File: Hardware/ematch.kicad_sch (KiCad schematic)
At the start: 33 parts, among them J3 Conn_01x02_Male, J4 Conn_01x02_Male, J5 Conn_01x02_Male, J6 Conn_01x02_Male, Q1 NCV8403, Q2 NCV8403, Q3 NCV8403, Q4 NCV8403, U6 LTV-247

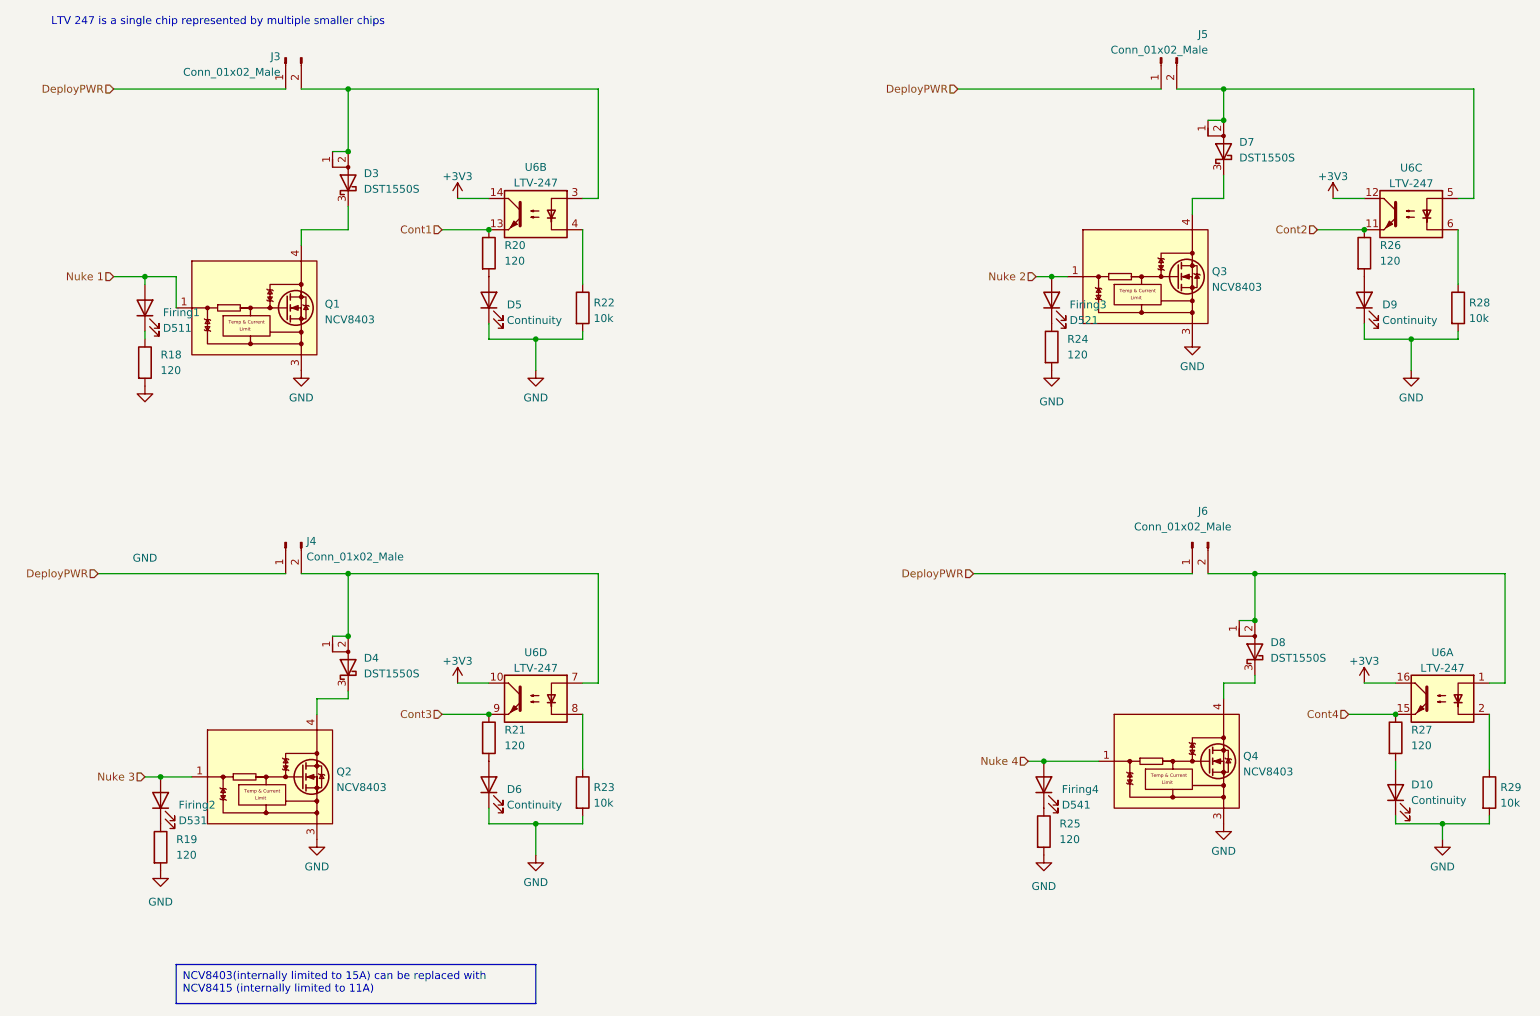
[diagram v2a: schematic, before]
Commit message: high V side finished, CAN circuit and ESP left to place
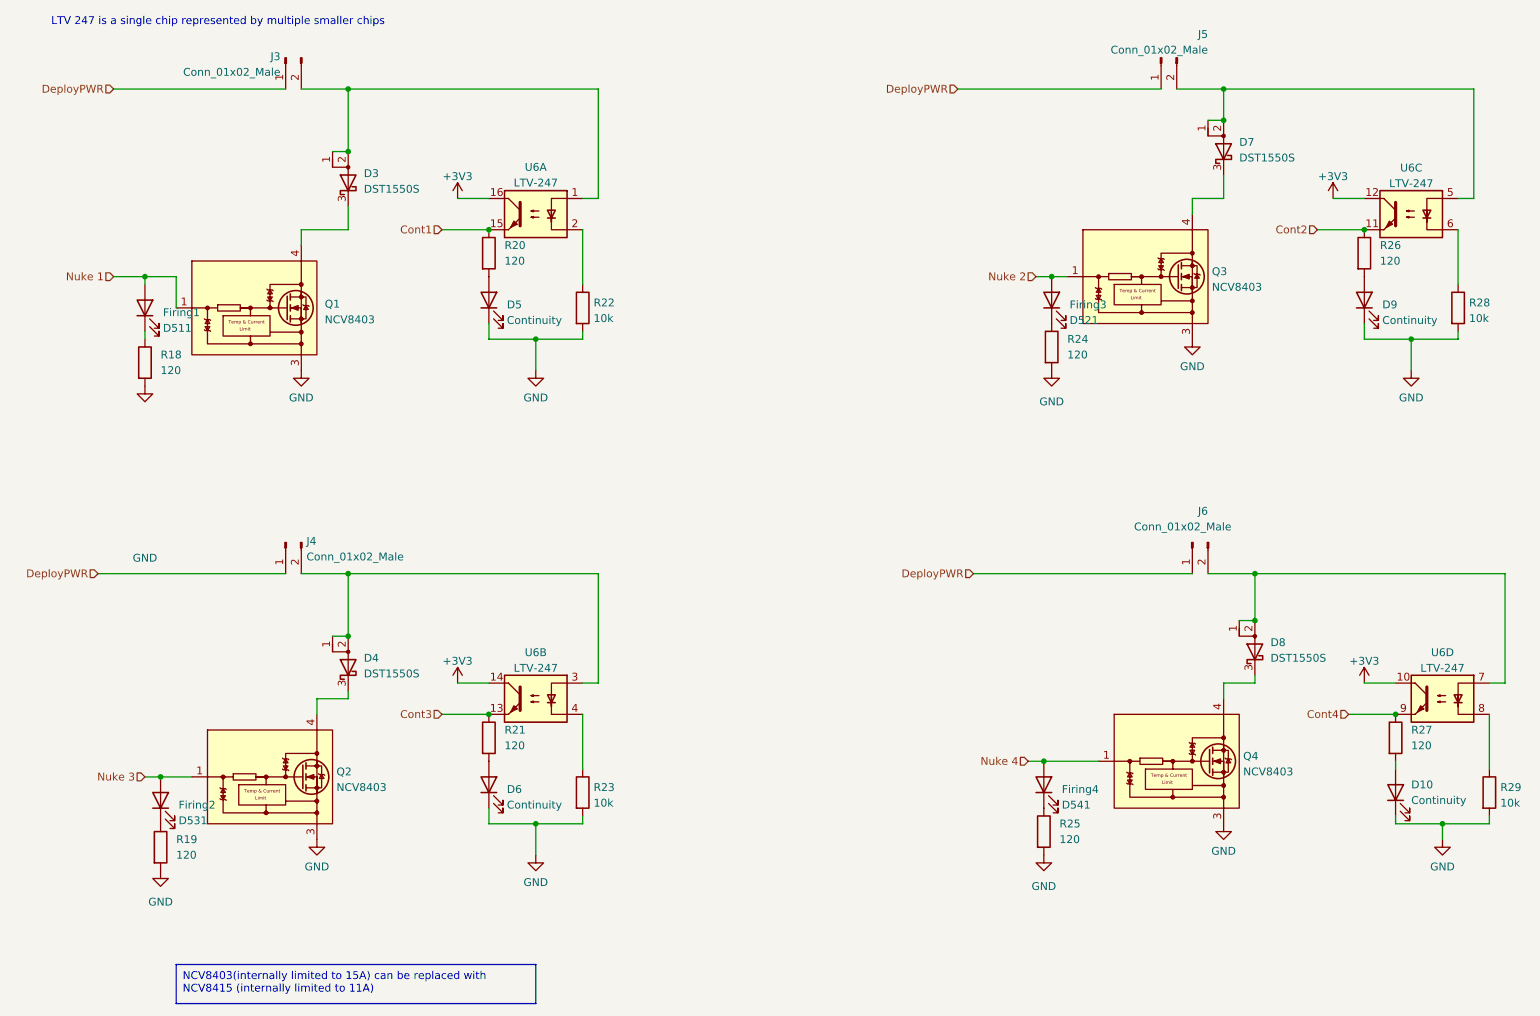
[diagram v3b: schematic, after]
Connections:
- net +3V3: now also U6.10, U6.14, U6.16; no longer U6.10, U6.14, U6.16
- net Cont1: now also U6.15; no longer U6.13
- net Cont3: now also U6.13; no longer U6.9
- net Cont4: now also U6.9; no longer U6.15
- net at D3.1 (A), D3.2 (A), J3.2 (Pin_2): now also U6.1; no longer U6.3
- net at D4.1 (A), D4.2 (A), J4.2 (Pin_2): now also U6.3; no longer U6.7
- net at D8.1 (A), D8.2 (A), J6.2 (Pin_2): now also U6.7; no longer U6.1
- net at R29.1: now also U6.8; no longer U6.2
- net at R23.1: now also U6.4; no longer U6.8
- net at R22.1: now also U6.2; no longer U6.4
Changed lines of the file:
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@@
     )
   )
-  (symbol (lib_id "Isolator:LTV-247") (at 243.84 129.54 0) (mirror y) (unit 1)
+  (symbol (lib_id "Isolator:LTV-247") (at 243.84 129.54 0) (mirror y) (unit 4)
     (in_bom yes) (on_board yes) (dnp no) (fields_autoplaced)
     (property "Reference" "U6" (at 243.84 122.0302 0)
@@
       (project "flintandsteel"
         (path "/7db990e4-92e1-4f99-b4d2-435bbec1ba83/b9a85f03-bf97-4e73-b79c-bd8547648cfe"
-          (reference "U6") (unit 1)
+          (reference "U6") (unit 4)
         )
       )
@@
     )
   )
-  (symbol (lib_id "Isolator:LTV-247") (at 96.52 50.8 0) (mirror y) (unit 2)
+  (symbol (lib_id "Isolator:LTV-247") (at 96.52 50.8 0) (mirror y) (unit 1)
     (in_bom yes) (on_board yes) (dnp no) (fields_autoplaced)
     (property "Reference" "U6" (at 96.52 43.18 0)
@@
       (project "flintandsteel"
         (path "/7db990e4-92e1-4f99-b4d2-435bbec1ba83/b9a85f03-bf97-4e73-b79c-bd8547648cfe"
-          (reference "U6") (unit 2)
+          (reference "U6") (unit 1)
         )
       )
@@
     )
   )
-  (symbol (lib_id "Isolator:LTV-247") (at 96.52 129.54 0) (mirror y) (unit 4)
+  (symbol (lib_id "Isolator:LTV-247") (at 96.52 129.54 0) (mirror y) (unit 2)
     (in_bom yes) (on_board yes) (dnp no) (fields_autoplaced)
     (property "Reference" "U6" (at 96.52 122.0302 0)
@@
       (project "flintandsteel"
         (path "/7db990e4-92e1-4f99-b4d2-435bbec1ba83/b9a85f03-bf97-4e73-b79c-bd8547648cfe"
-          (reference "U6") (unit 4)
-        )
-      )
+          (reference "U6") (unit 2)
+        )
+      )

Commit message: finished? (pre-review)
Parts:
- renumbered D7 to D4, D4 to D7
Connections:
- net Cont2: now also R21.1, U6.13; no longer R26.1, U6.11
- net Cont3: now also R26.1, U6.11; no longer R21.1, U6.13
- net Nuke 2: now also Firing2.2 (A), Q2.1 (G); no longer Firing3.2 (A), Q3.1 (G)
- net Nuke 3: now also Firing3.2 (A), Q3.1 (G); no longer Firing2.2 (A), Q2.1 (G)
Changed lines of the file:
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@@
     (effects (font (size 1.27 1.27)) (justify left bottom))
   )
-  (hierarchical_label "Cont3" (shape input) (at 81.28 132.08 180) (fields_autoplaced)
+  (hierarchical_label "Cont2" (shape input) (at 81.28 132.08 180) (fields_autoplaced)
     (effects (font (size 1.27 1.27)) (justify right))
   )
-  (hierarchical_label "Cont2" (shape input) (at 223.52 53.34 180) (fields_autoplaced)
+  (hierarchical_label "Cont3" (shape input) (at 223.52 53.34 180) (fields_autoplaced)
     (effects (font (size 1.27 1.27)) (justify right))
   )
@@
     (effects (font (size 1.27 1.27)) (justify right))
   )
-  (hierarchical_label "Nuke 3" (shape input) (at 33.02 142.24 180) (fields_autoplaced)
+  (hierarchical_label "Nuke 2" (shape input) (at 33.02 142.24 180) (fields_autoplaced)
     (effects (font (size 1.27 1.27)) (justify right))
   )
@@
     (effects (font (size 1.27 1.27)) (justify right))
   )
-  (hierarchical_label "Nuke 2" (shape input) (at 177.8 60.96 180) (fields_autoplaced)
+  (hierarchical_label "Nuke 3" (shape input) (at 177.8 60.96 180) (fields_autoplaced)
     (effects (font (size 1.27 1.27)) (justify right))
   )
@@
   (symbol (lib_id "Device:D_Schottky_AAK") (at 208.28 40.64 90) (unit 1)
     (in_bom yes) (on_board yes) (dnp no) (fields_autoplaced)
-    (property "Reference" "D7" (at 210.82 39.116 90)
+    (property "Reference" "D4" (at 210.82 39.116 90)
       (effects (font (size 1.27 1.27)) (justify right))
     )
@@
       (project "flintandsteel"
         (path "/7db990e4-92e1-4f99-b4d2-435bbec1ba83/b9a85f03-bf97-4e73-b79c-bd8547648cfe"
-          (reference "D7") (unit 1)
+          (reference "D4") (unit 1)
         )
       )
@@
   (symbol (lib_id "Device:LED") (at 35.56 146.05 90) (unit 1)
     (in_bom yes) (on_board yes) (dnp no) (fields_autoplaced)
-    (property "Reference" "Firing2" (at 38.481 146.8028 90)
-      (effects (font (size 1.27 1.27)) (justify right))
-    )
-    (property "Value" "D531" (at 38.481 149.3397 90)
+    (property "Reference" "Firing2" (at 39.37 147.0025 90)
+      (effects (font (size 1.27 1.27)) (justify right))
+    )
+    (property "Value" "D531" (at 39.37 149.5425 90)
       (effects (font (size 1.27 1.27)) (justify right))
     )
@@
   (symbol (lib_id "Driver_FET:NCV8402xST") (at 53.34 142.24 0) (unit 1)
     (in_bom yes) (on_board yes) (dnp no) (fields_autoplaced)
-    (property "Reference" "Q2" (at 64.135 141.4053 0)
-      (effects (font (size 1.27 1.27)) (justify left))
-    )
-    (property "Value" "NCV8403" (at 64.135 143.9422 0)
+    (property "Reference" "Q2" (at 64.77 141.605 0)
+      (effects (font (size 1.27 1.27)) (justify left))
+    )
+    (property "Value" "NCV8403" (at 64.77 144.145 0)
       (effects (font (size 1.27 1.27)) (justify left))
     )
@@
   (symbol (lib_id "Device:D_Schottky_AAK") (at 66.04 124.46 90) (unit 1)
     (in_bom yes) (on_board yes) (dnp no) (fields_autoplaced)
-    (property "Reference" "D4" (at 68.58 122.936 90)
+    (property "Reference" "D7" (at 68.58 122.936 90)
       (effects (font (size 1.27 1.27)) (justify right))
     )
@@
       (project "flintandsteel"
         (path "/7db990e4-92e1-4f99-b4d2-435bbec1ba83/b9a85f03-bf97-4e73-b79c-bd8547648cfe"
-          (reference "D4") (unit 1)
+          (reference "D7") (unit 1)
         )
       )
@@
   (symbol (lib_id "Driver_FET:NCV8402xST") (at 195.58 60.96 0) (unit 1)
     (in_bom yes) (on_board yes) (dnp no) (fields_autoplaced)
-    (property "Reference" "Q3" (at 206.375 60.1253 0)
-      (effects (font (size 1.27 1.27)) (justify left))
-    )
-    (property "Value" "NCV8403" (at 206.375 62.6622 0)
+    (property "Reference" "Q3" (at 207.01 60.325 0)
+      (effects (font (size 1.27 1.27)) (justify left))
+    )
+    (property "Value" "NCV8403" (at 207.01 62.865 0)
       (effects (font (size 1.27 1.27)) (justify left))
     )
@@
   (symbol (lib_id "Device:LED") (at 180.34 64.77 90) (unit 1)
     (in_bom yes) (on_board yes) (dnp no) (fields_autoplaced)
-    (property "Reference" "Firing3" (at 183.261 65.5228 90)
-      (effects (font (size 1.27 1.27)) (justify right))
-    )
-    (property "Value" "D521" (at 183.261 68.0597 90)
-      (effects (font (size 1.27 1.27)) (justify right))
-    )
+    (property "Reference" "Firing3" (at 184.15 65.7225 90)
+      (effects (font (size 1.27 1.27)) (justify right))
+    )
+    (property "Value" "D521" (at 184.15 68.2625 90)
+      (effects (font (size 1.27 1.27)) (justify right))
+    )

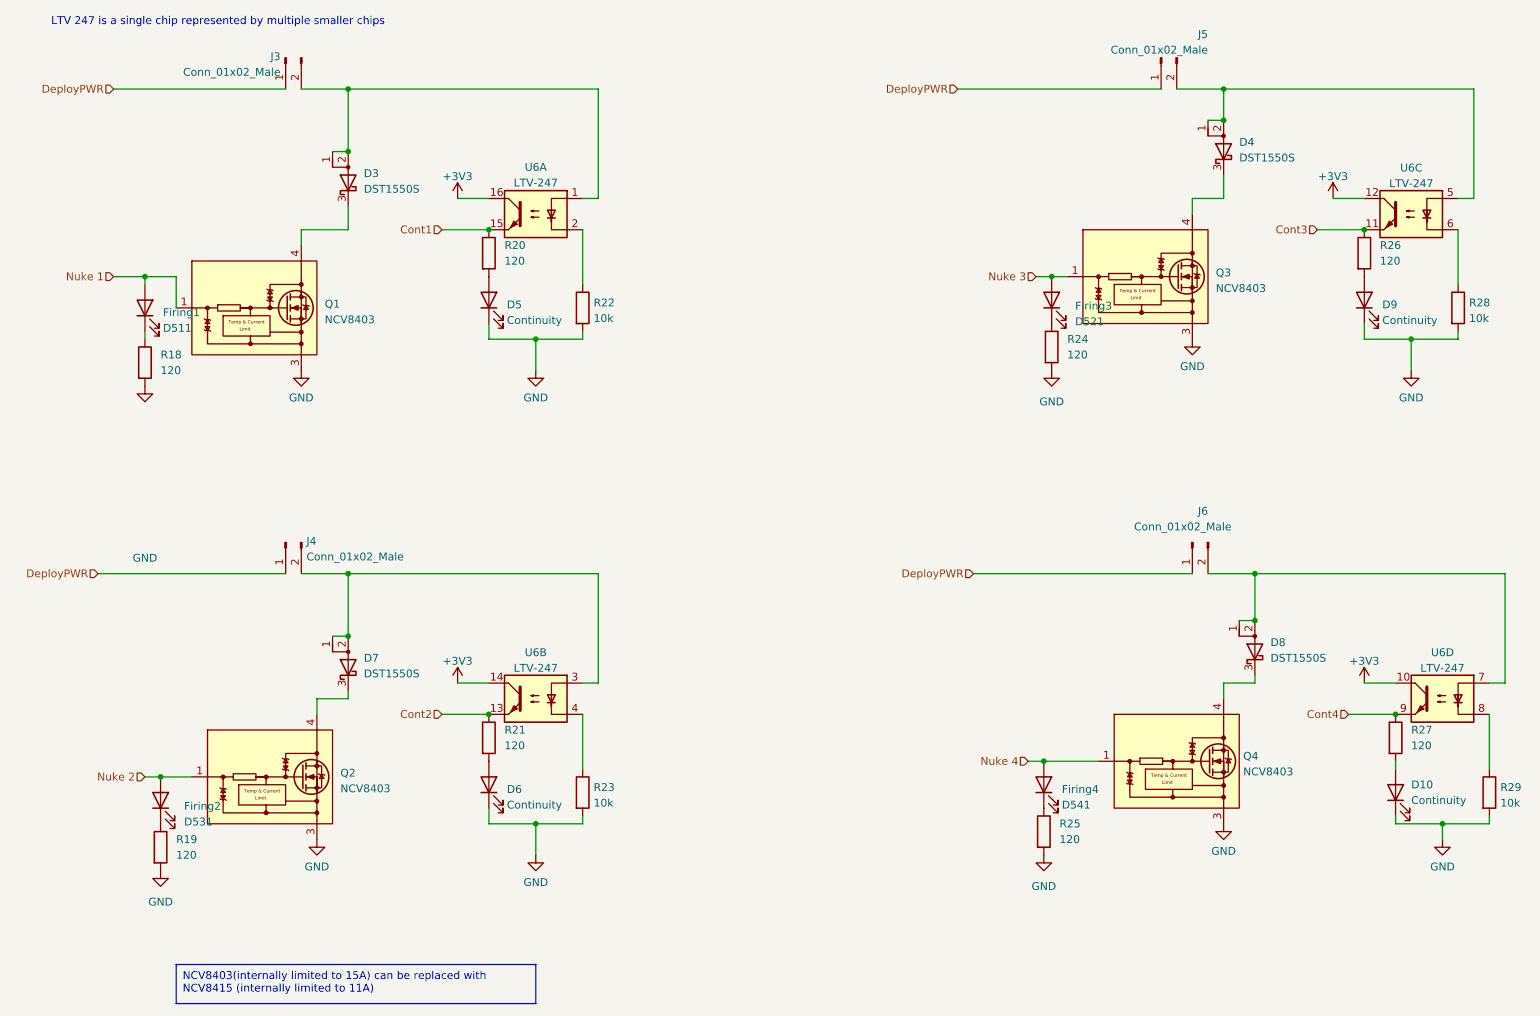
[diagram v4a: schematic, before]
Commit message: changed mosfets and added current sense circuit, layout not done
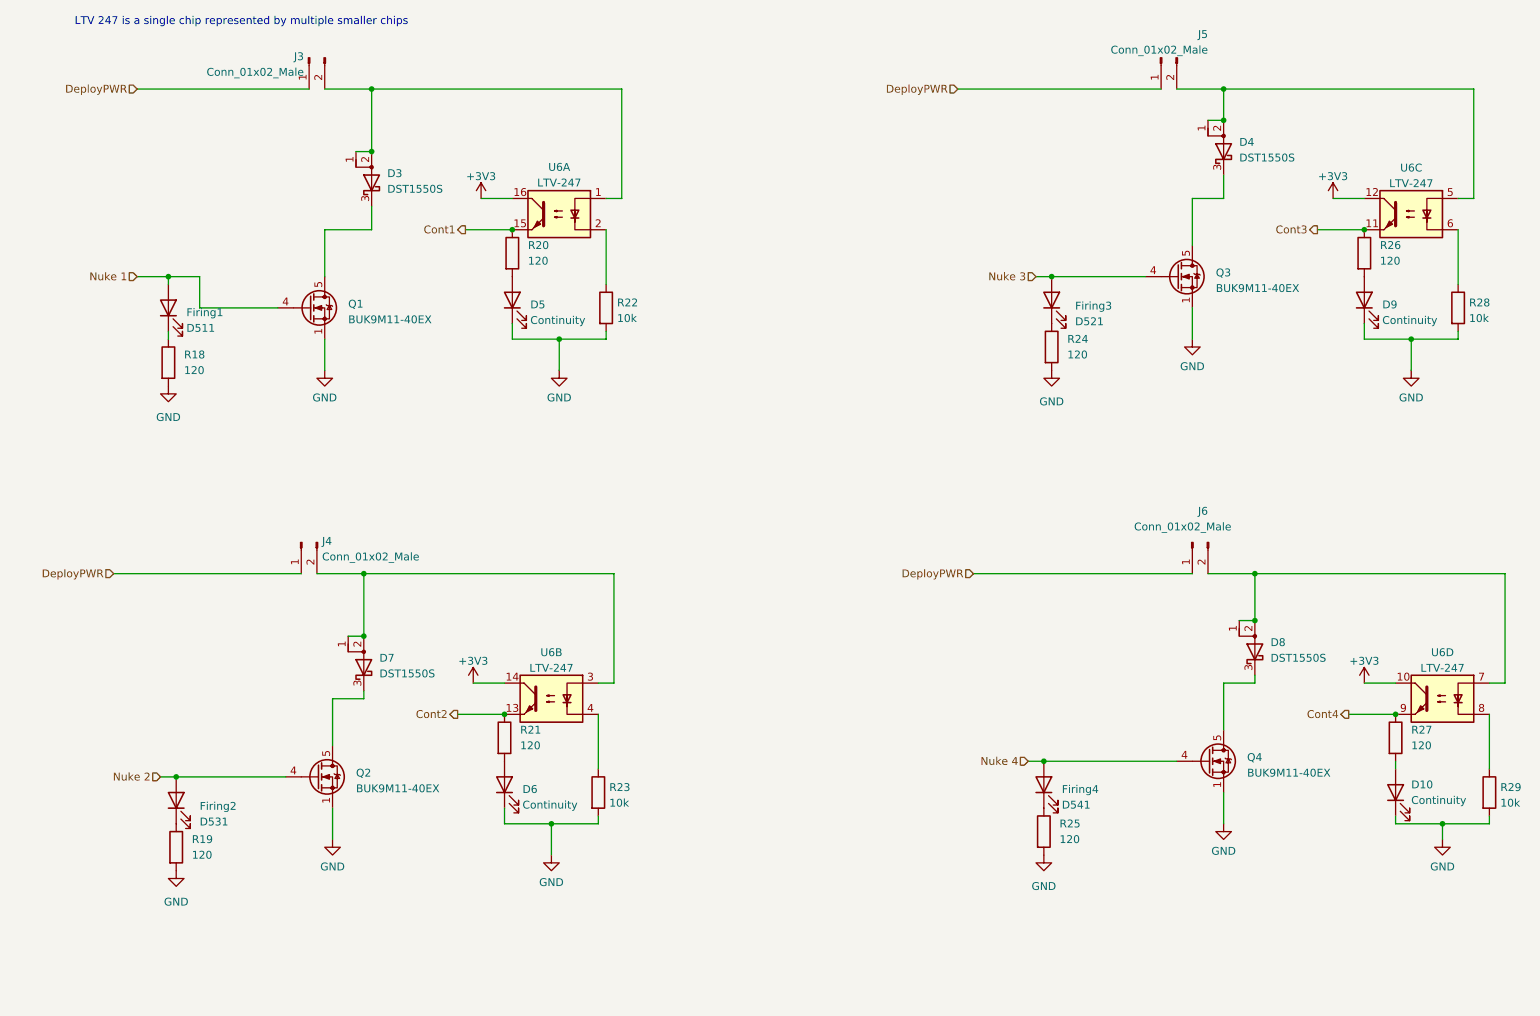
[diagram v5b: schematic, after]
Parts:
- removed Q1, Q2, Q3, Q4: NCV8403, Package_TO_SOT_SMD:SOT-223, symbol Driver_FET:NCV8402xST
- added Q1, Q2, Q3, Q4: BUK9M11-40EX, Package_TO_SOT_SMD:LFPAK33, symbol Transistor_FET:BUK9M11-40EX
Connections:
- net GND: now also Q1.1 (S), Q1.2 (S), Q1.3 (S), Q2.1 (S), Q2.2 (S), Q2.3 (S), Q3.1 (S), Q3.2 (S), Q3.3 (S), Q4.1 (S), Q4.2 (S), Q4.3 (S)
- net Nuke 1: now also Q1.4 (G)
- net Nuke 2: now also Q2.4 (G)
- net Nuke 3: now also Q3.4 (G)
- net Nuke 4: now also Q4.4 (G)
- net at D3.3 (K): now also Q1.5 (D)
- net at D4.3 (K): now also Q3.5 (D)
- net at D7.3 (K): now also Q2.5 (D)
- net at D8.3 (K): now also Q4.5 (D)
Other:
- moved on the sheet: D3, D5, D6, D7, Firing1, Firing2, J3, J4, R18, R19, R20, R21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
